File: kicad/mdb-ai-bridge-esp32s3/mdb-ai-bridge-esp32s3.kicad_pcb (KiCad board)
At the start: 2 copper layers, 130.3 x 40 mm, 94 parts, among them J3 Conn_02x08_Top_Bottom, J7 USB_C_Receptacle_USB2.0_16P, SW3 SW_Push, SW4 SW_Push, SW5 SW_Push, SW6 SW_Push, SW7 SW_Push, SW8 SW_Push, SW9 SW_Push, U10 ESP32-S3FH4R2, U11 ESP32-S3FH4R2, U12 ESP32-S3FH4R2, U13 AMS1117-3.3, U14 USB2514B_Bi, Y2 Crystal_GND24, Y3 Crystal_GND24, Y4 Crystal_GND24, Y5 Crystal_GND24

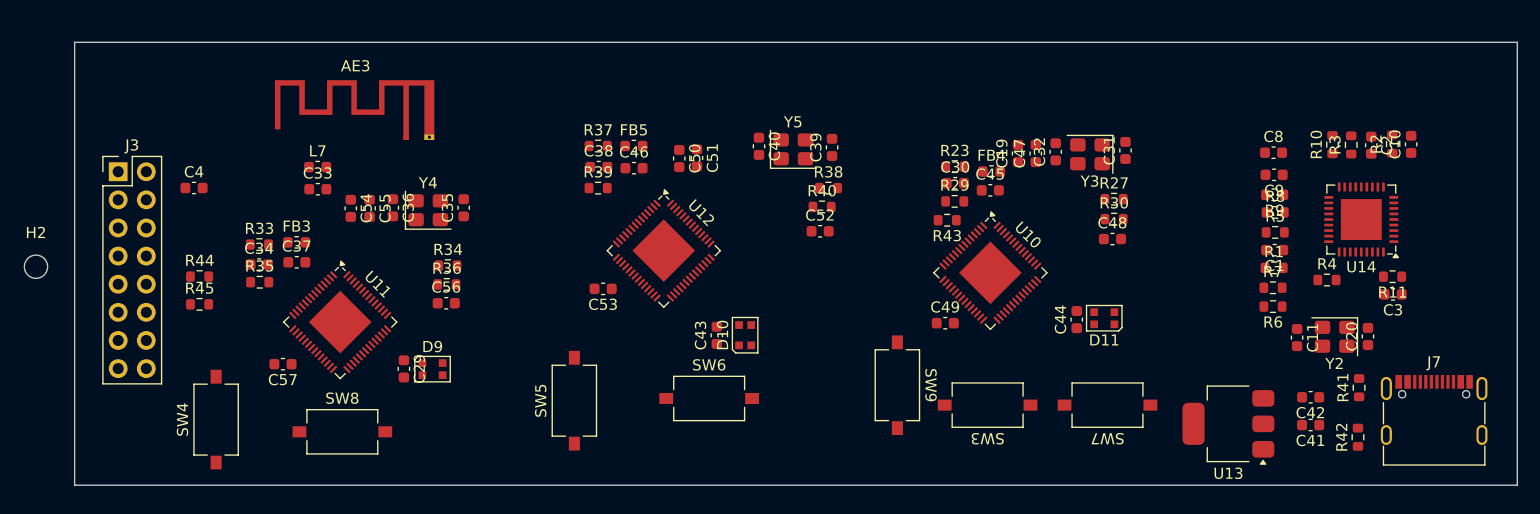
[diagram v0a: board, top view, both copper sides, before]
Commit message: fix(hardware): update LCSC# and values in mdb-bridge-esp32s3 schematic
- C3: Value "?" → "1uF", LCSC# → C696901 (AP2112K-3.3 input cap)
- C1, C2, C15: LCSC# C6119849 → C696901 (discontinued → active 1uF 16V X5R 0603)
- C32: Value "220uF" → "100uF", LCSC# → C90975 (LM2594HVM-5V output, 10V CASE-B derating)

Co-Authored-By: Claude Sonnet 4.6 <noreply@anthropic.com>
Claude-Session: https://claude.ai/code/session_01Qh1XTvg8Um6L2D2gYWdT7R
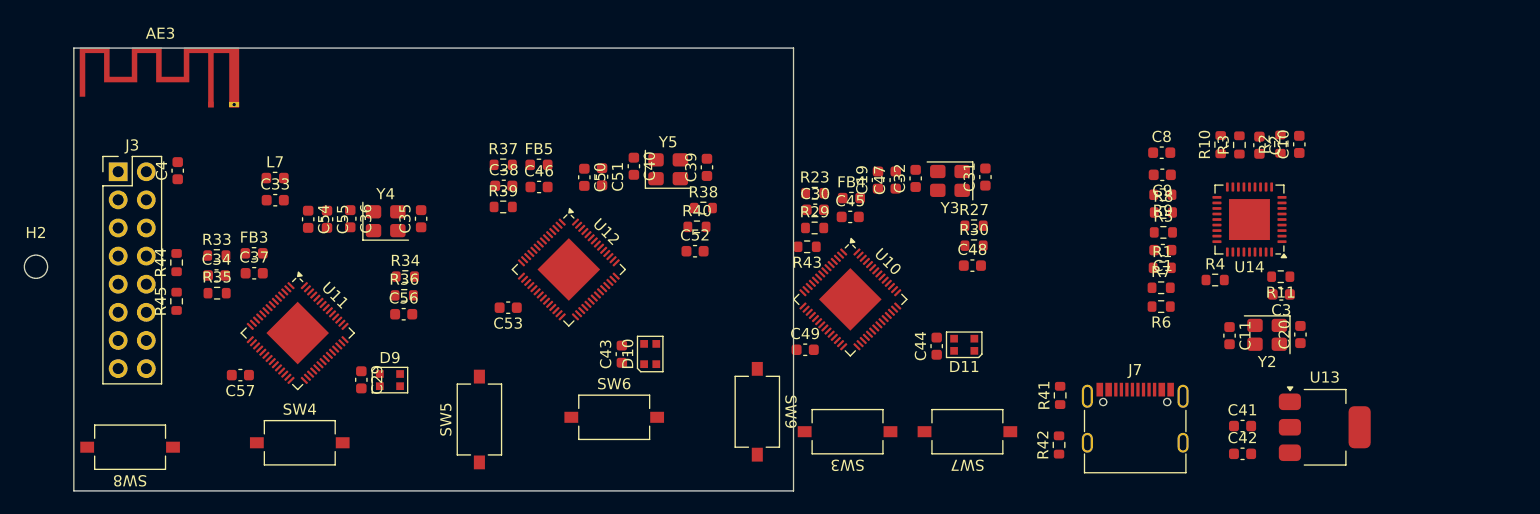
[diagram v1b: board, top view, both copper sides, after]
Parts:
- moved J7 27.0 mm to (227.3, 109.3)
- moved R41 27.0 mm to (220.5, 106.1)
- moved R42 27.0 mm to (220.4, 110.6)
- moved SW8 19.2 mm to (136.5, 110.8), turned to 180 degrees
- moved AE3 17.9 mm to (143.8, 79.9)
- moved C30 12.9 mm to (198.4, 89.4)
- moved C31 12.9 mm to (213.8, 86.4)
- moved C32 12.9 mm to (207.4, 86.5)
- moved C45 12.9 mm to (201.5, 90.0)
- moved C48 12.9 mm to (212.6, 94.4)
- moved C49 12.9 mm to (197.5, 102.0)
- moved R23 12.9 mm to (198.3, 87.9)
- moved R29 12.9 mm to (198.3, 91.0)
- moved R43 12.9 mm to (197.7, 92.7)
- moved SW7 12.9 mm to (212.1, 109.4)
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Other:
- board size 130.3 x 40 mm -> 65 x 40 mm
